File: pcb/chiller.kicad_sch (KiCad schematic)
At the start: 56 parts, among them J1 Temp sensor 1, J10 Current Sense, J11 Display, J12 Debug, J13 Conn_01x04, J14 Flow sensor, J15 Fan, J2 Temp sensor 2, J3 Ext, J4 Mains in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

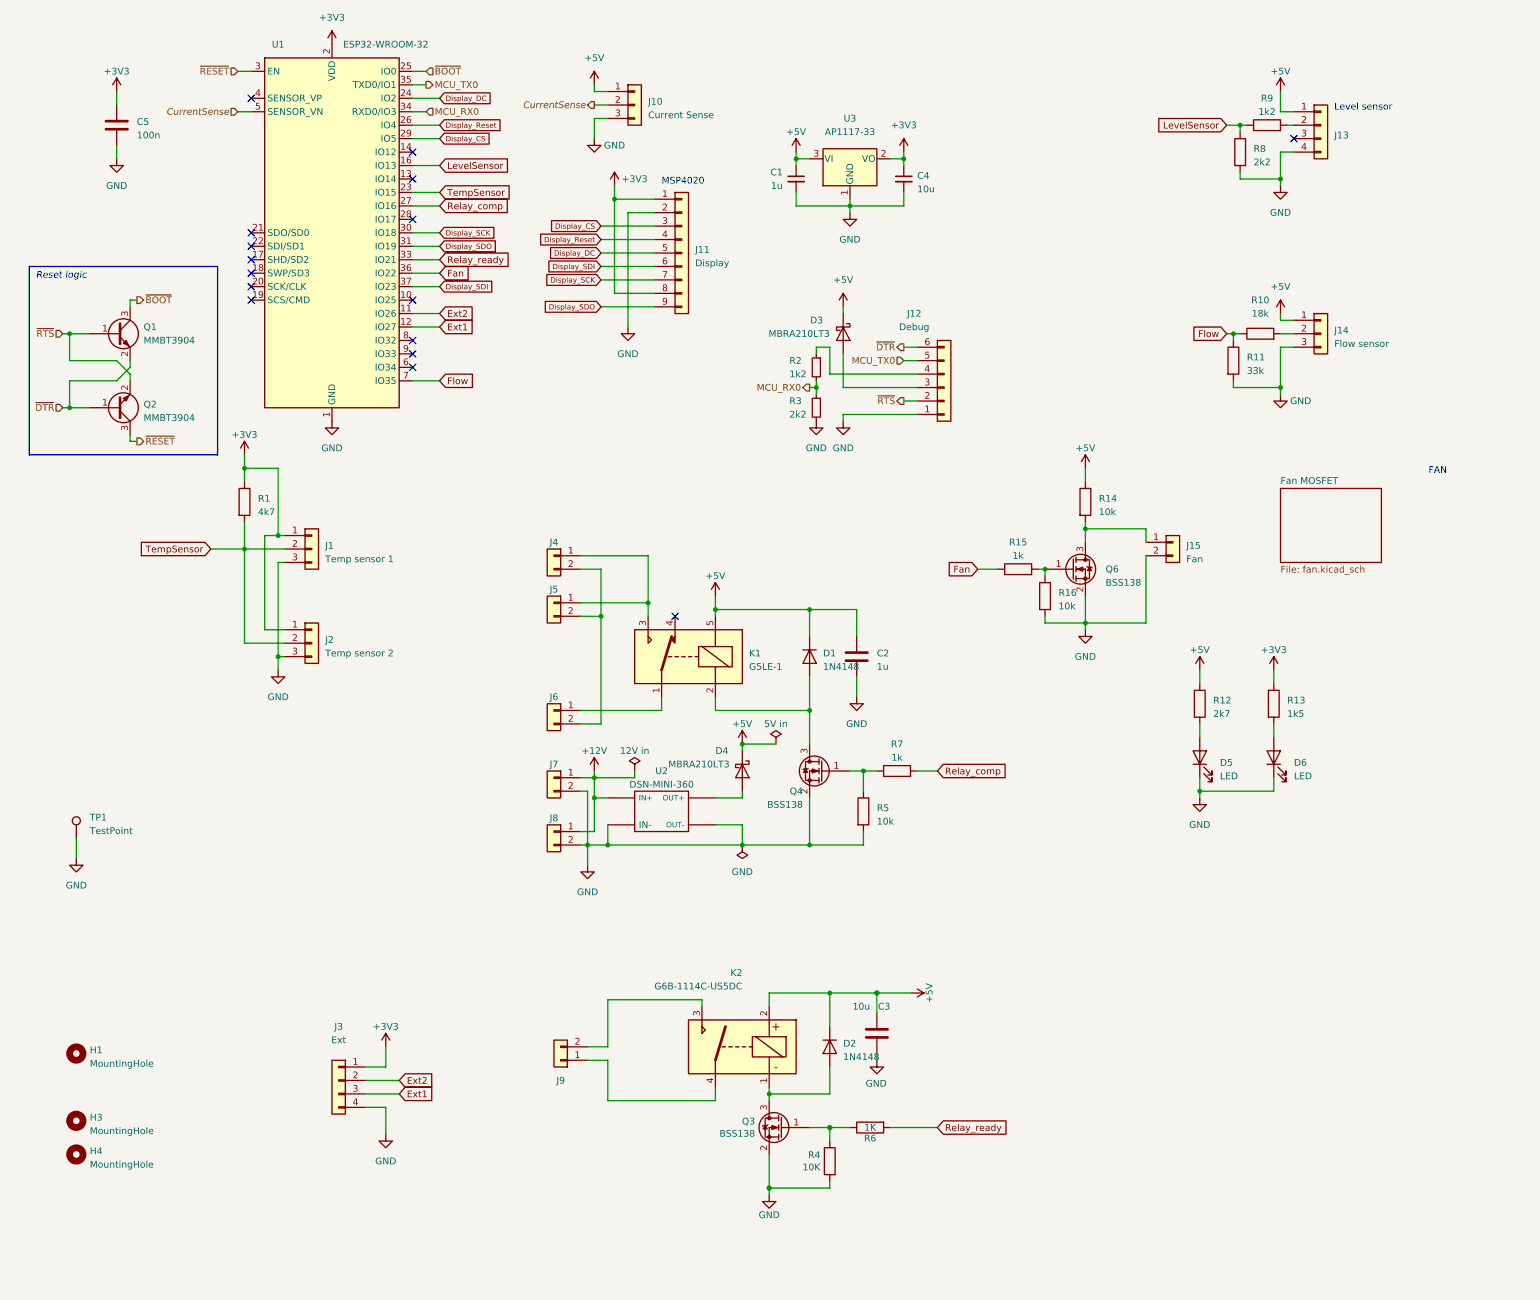
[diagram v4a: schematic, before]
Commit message: Add BOOT switch
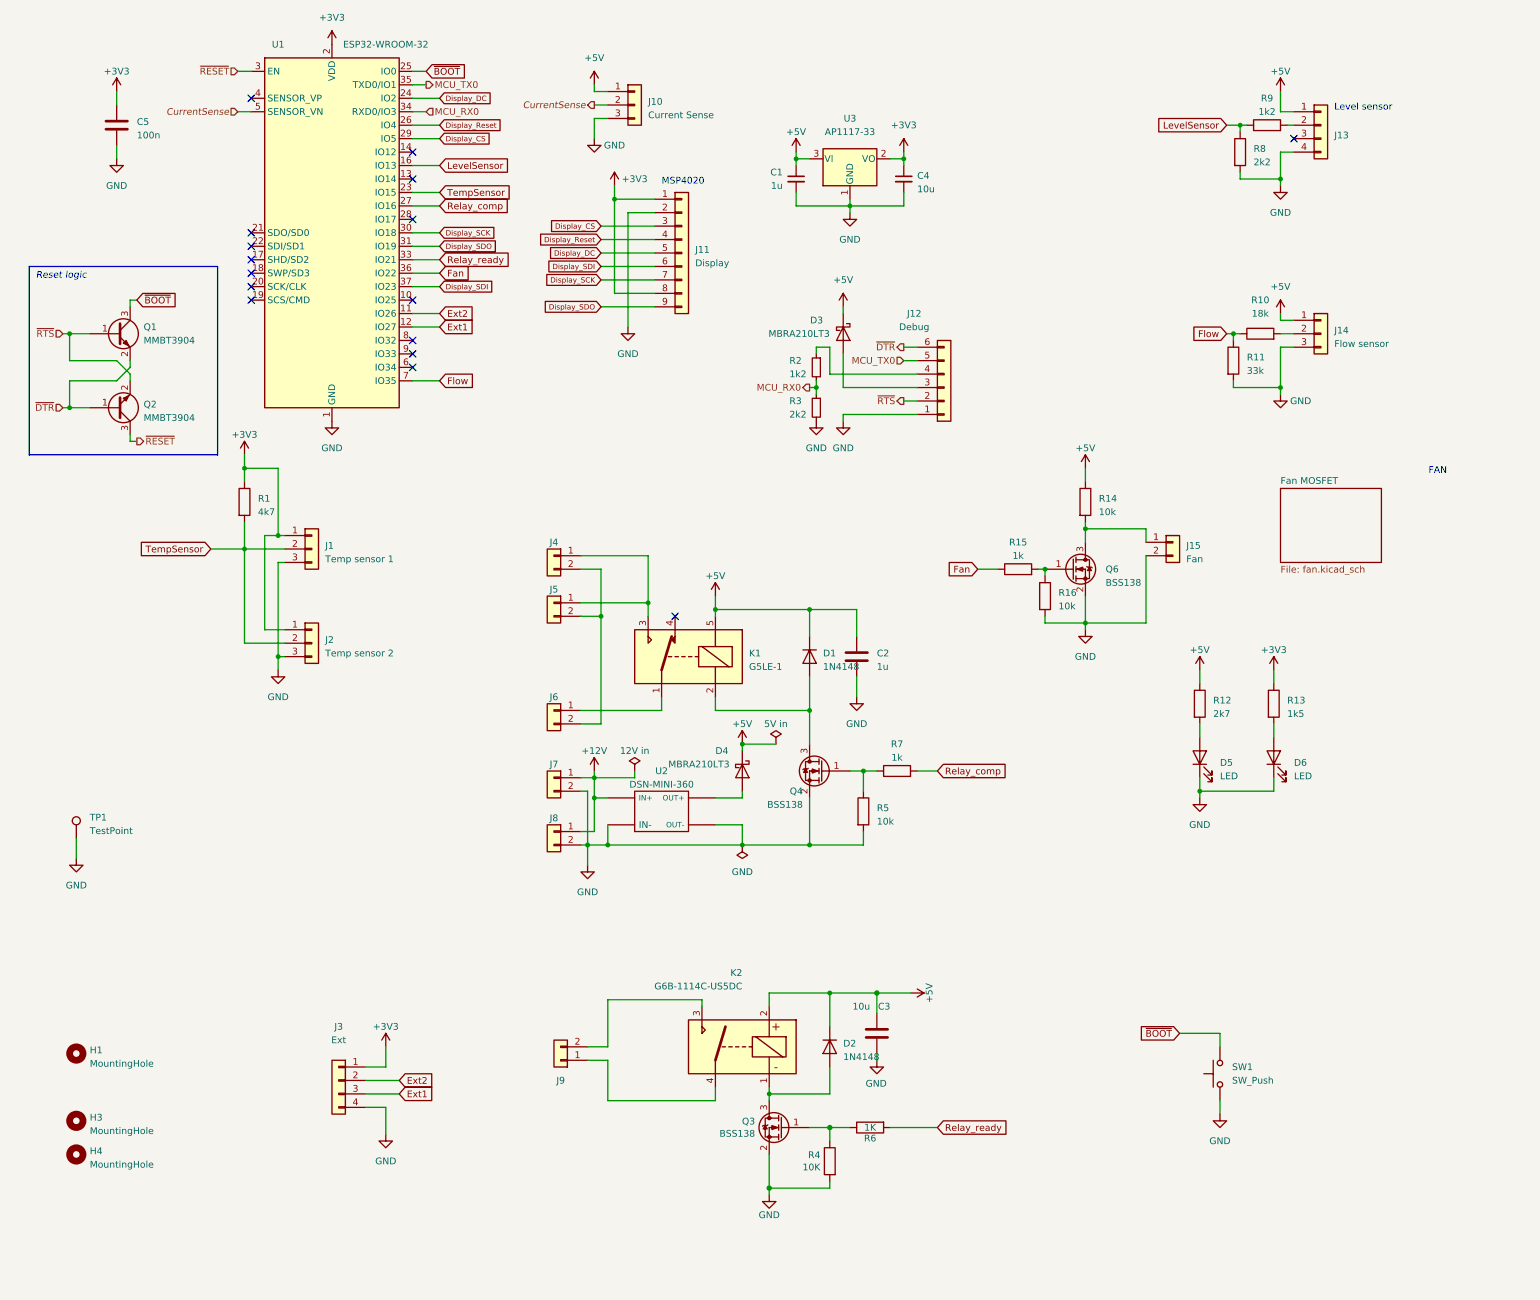
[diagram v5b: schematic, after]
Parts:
- added SW1: SW_Push, symbol Switch:SW_Push
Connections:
- net GND: now also SW1.1
- net ~{BOOT}: now also SW1.2
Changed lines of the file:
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@@
+    (stroke (width 0) (type default))
+  )
+  (wire (pts (xy 241.3 210.82) (xy 233.68 210.82))
     (stroke (width 0) (type default))
   )
@@
     (stroke (width 0) (type default))
   )
+  (wire (pts (xy 241.3 213.36) (xy 241.3 210.82))
+    (stroke (width 0) (type default))
+  )
   (wire (pts (xy 35.56 72.39) (xy 36.83 72.39))
     (stroke (width 0) (type default))
@@
   (wire (pts (xy 187.96 228.6) (xy 179.07 228.6))
     (stroke (width 0) (type solid))
+  )
+  (wire (pts (xy 241.3 223.52) (xy 241.3 226.06))
+    (stroke (width 0) (type default))
   )
   (wire (pts (xy 252.73 88.9) (xy 252.73 90.17))
@@
  (at 280.67 105.41 0)
     (effects (font (size 1.27 1.27)) (justify left bottom))
+  )
+  (global_label "~{BOOT}" (shape input) (at 36.83 72.39 0) (fields_autoplaced)
+    (effects (font (size 1.27 1.27)) (justify left))
+    (property "Intersheetrefs" "${INTERSHEET_REFS}" (at 44.7138 72.39 0)
+      (effects (font (size 1.27 1.27)) (justify left) hide)
+    )
   )
   (global_label "Relay_comp" (shape input) (at 93.98 54.61 0) (fields_autoplaced)
@@
     )
   )
+  (global_label "~{BOOT}" (shape input) (at 91.44 29.21 0) (fields_autoplaced)
+    (effects (font (size 1.27 1.27)) (justify left))
+    (property "Intersheetrefs" "${INTERSHEET_REFS}" (at 99.3238 29.21 0)
+      (effects (font (size 1.27 1.27)) (justify left) hide)
+    )
+  )
   (global_label "Display_Reset" (shape input) (at 93.98 39.37 0) (fields_autoplaced)
     (effects (font (size 1 1)) (justify left))
@@
     )
   )
+  (global_label "~{BOOT}" (shape input) (at 233.68 210.82 180) (fields_autoplaced)
+    (effects (font (size 1.27 1.27)) (justify right))
+    (property "Intersheetrefs" "${INTERSHEET_REFS}" (at 225.7962 210.82 0)
+      (effects (font (size 1.27 1.27)) (justify right) hide)
+    )
+  )
   (global_label "Display_DC" (shape input) (at 124.46 63.5 180) (fields_autoplaced)
     (effects (font (size 1 1)) (justify right))
@@
     (effects (font (size 1.27 1.27)) (justify right))
   )
-  (hierarchical_label "~{BOOT}" (shape output) (at 36.83 72.39 0) (fields_autoplaced)
-    (effects (font (size 1.27 1.27)) (justify left))
-  )
   (hierarchical_label "MCU_RX0" (shape output) (at 163.83 88.9 180) (fields_autoplaced)
     (effects (font (size 1.27 1.27)) (justify right))
@@
   (hierarchical_label "~{RTS}" (shape output) (at 181.61 91.44 180) (fields_autoplaced)
     (effects (font (size 1.27 1.27)) (justify right))
-  )
-  (hierarchical_label "~{BOOT}" (shape input) (at 91.44 29.21 0) (fields_autoplaced)
-    (effects (font (size 1.27 1.27)) (justify left))
   )
   (hierarchical_label "~{RTS}" (shape input) (at 22.86 78.74 180) (fields_autoplaced)
@@
     )
   )
+  (symbol (lib_id "Switch:SW_Push") (at 241.3 218.44 90) (unit 1)
+    (exclude_from_sim no) (in_bom yes) (on_board yes) (dnp no) (fields_autoplaced)
+    (property "Reference" "SW1" (at 243.586 217.1699 90)
+      (effects (font (size 1.27 1.27)) (justify right))
+    )
+    (property "Value" "SW_Push" (at 243.586 219.7099 90)
+      (effects (font (size 1.27 1.27)) (justify right))
+    )
+    (property "Footprint" "" (at 236.22 218.44 0)
+      (effects (font (size 1.27 1.27)) hide)
+    )
+    (property "Datasheet" "~" (at 236.22 218.44 0)
+      (effects (font (size 1.27 1.27)) hide)
+    )
+    (property "Description" "Push button switch, generic, two pins" (at 241.3 218.44 0)
+      (effects (font (size 1.27 1.27)) hide)
+    )
+    (pin "1")
+    (pin "2")
+    (instances
+      (project "chiller"
+        (path "/212a0d71-cc7b-49f8-b4ca-a935e5355dca"
+          (reference "SW1") (unit 1)
+        )
+      )
+    )
+  )
   (symbol (lib_id "Device:R_Small") (at 165.1 85.09 0) (mirror y) (unit 1)
     (exclude_from_sim no) (in_bom yes) (on_board yes) (dnp no)
@@
       (effects (font (size 1.27 1.27)) hide)
     )
-    (property "Description" "" (at 135.89 168.91 0)
+    (property "Description" "Linear Regulator +5V" (at 135.89 168.91 0)
       (effects (font (size 1.27 1.27)) hide)
     )
@@
         )
       )
+    )
+  )
+  (symbol (lib_id "power:GND") (at 241.3 226.06 0) (unit 1)
+    (exclude_from_sim no) (in_bom yes) (on_board yes) (dnp no) (fields_autoplaced)
+    (property "Reference" "#PWR035" (at 241.3 232.41 0)
+      (effects (font (size 1.27 1.27)) hide)
+    )
+    (property "Value" "GND" (at 241.3 231.14 0)
+      (effects (font (size 1.27 1.27)))
+    )
+    (property "Footprint" "" (at 241.3 226.06 0)
+      (effects (font (size 1.27 1.27)) hide)
+    )
+    (property "Datasheet" "" (at 241.3 226.06 0)
+      (effects (font (size 1.27 1.27)) hide)
+    )
+    (property "Description" "Power flag, ground" (at 241.3 226.06 0)
+      (effects (font (size 1.27 1.27)) hide)
+    )
+    (pin "1")
+    (instances
+      (project "chiller"
+        (path "/212a0d71-cc7b-49f8-b4ca-a935e5355dca"
+          (reference "#PWR035") (unit 1)
+        )
+      )

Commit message: Add addon board.
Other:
- removed sheet Fan MOSFET
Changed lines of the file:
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@@
-    )
-  )
-  (sheet (at 252.73 107.95) (size 19.05 13.97) (fields_autoplaced)
-    (stroke (width 0.1524) (type solid))
-    (fill (color 0 0 0 0.0000))
-    (property "Sheetname" "Fan MOSFET" (at 252.73 107.2384 0)
-      (effects (font (size 1.27 1.27)) (justify left bottom))
-    )
-    (property "Sheetfile" "fan.kicad_sch" (at 252.73 122.5046 0)
-      (effects (font (size 1.27 1.27)) (justify left top))
-    )
-    (instances
-      (project "chiller"
-        (path "/212a0d71-cc7b-49f8-b4ca-a935e5355dca" (page "2"))
-      )
     )
   )

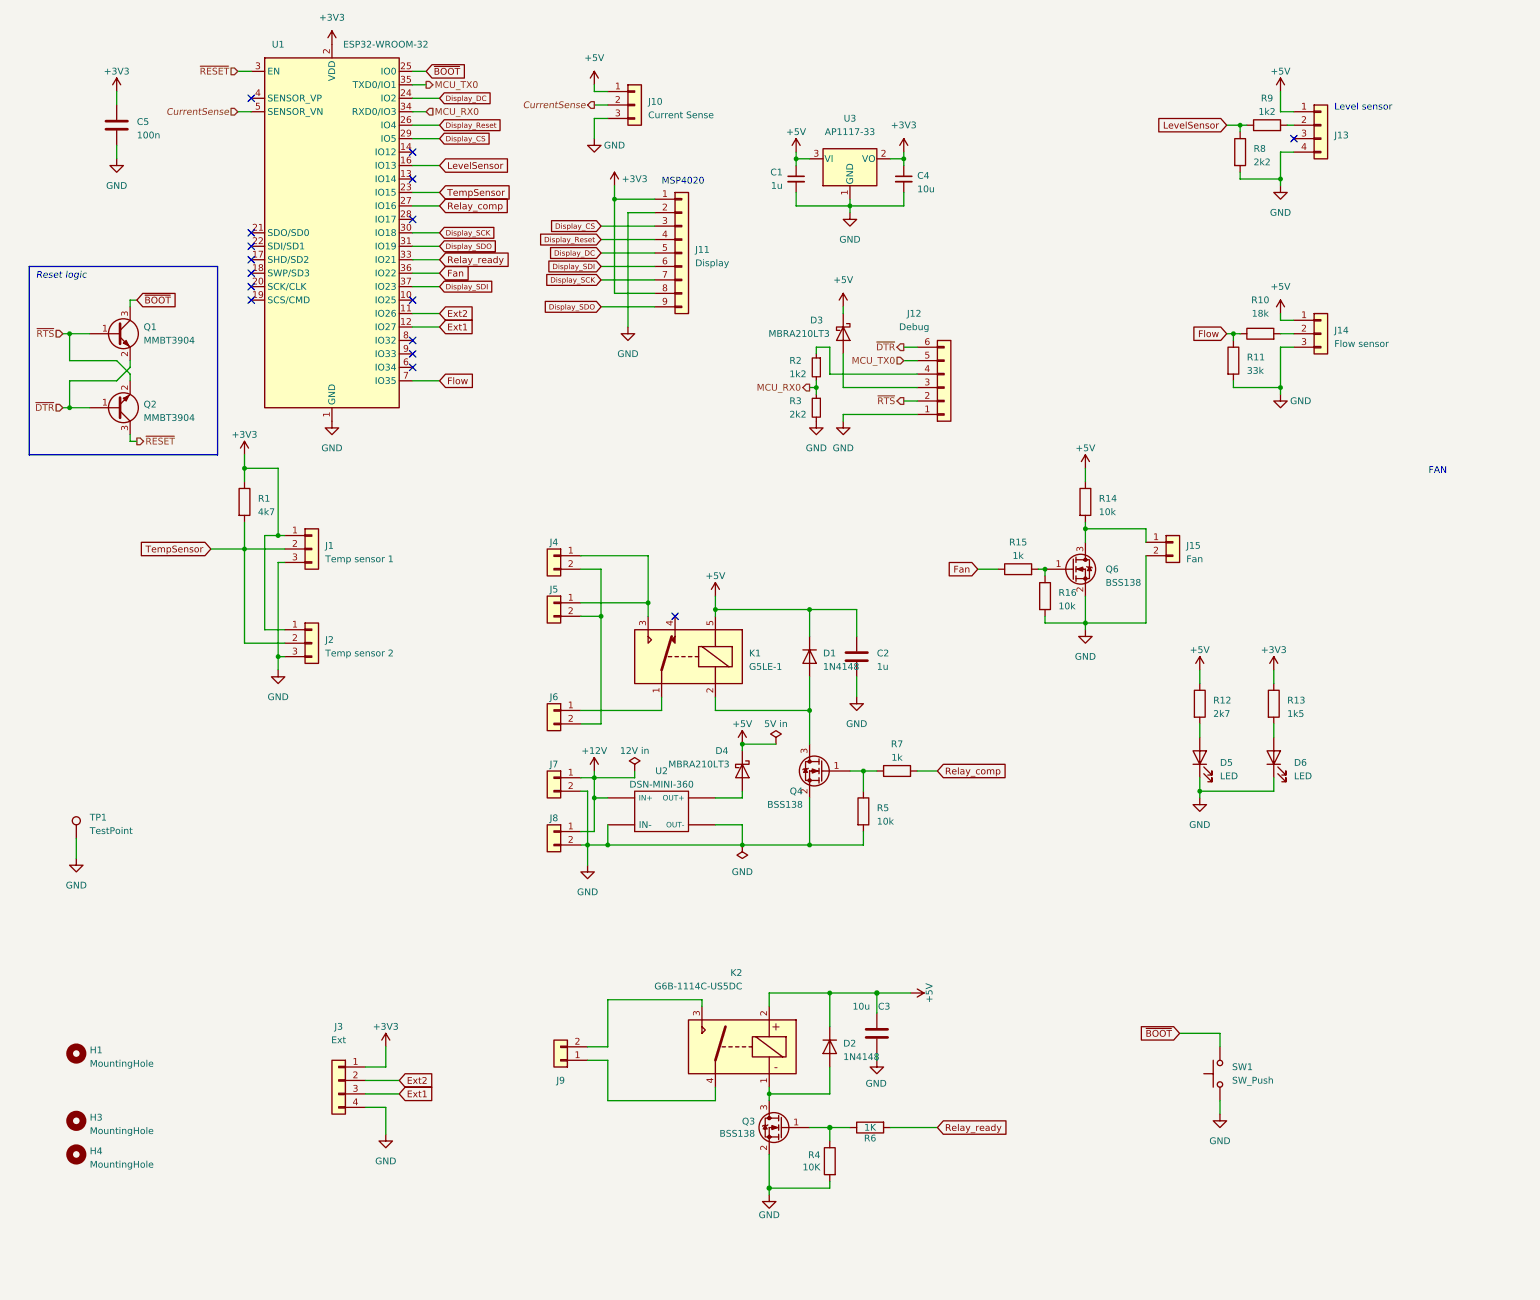
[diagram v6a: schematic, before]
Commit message: Move fan and buzzer MOSFETs onto main board.
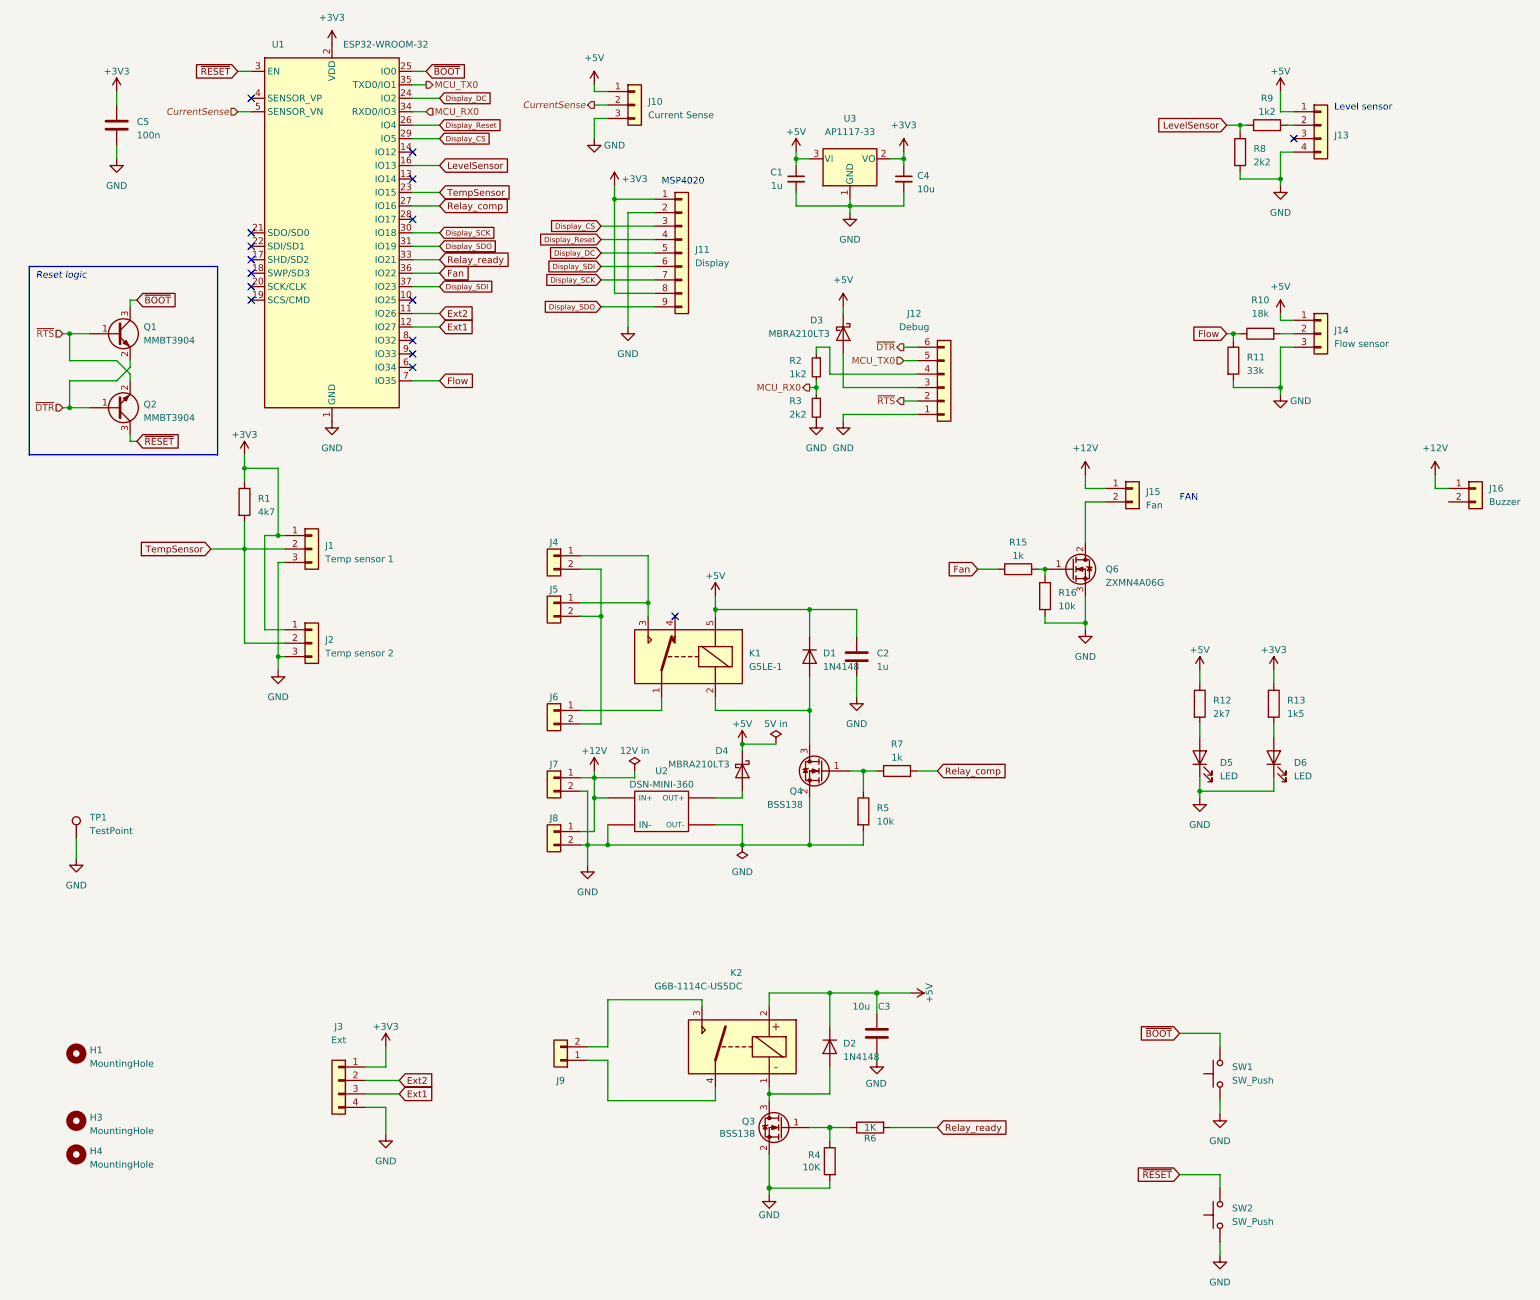
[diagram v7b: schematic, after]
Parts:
- removed R14: 10k, Resistor_SMD:R_0603_1608Metric, symbol Device:R
- added J16: Buzzer, symbol Connector_Generic:Conn_01x02
- added SW2: SW_Push, symbol Switch:SW_Push
- Q6: value BSS138 -> ZXMN4A06G; symbol Device:Q_NMOS_GSD -> Device:Q_NMOS_GDS
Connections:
- net +12V: now also J15.1 (Pin_1), J16.1 (Pin_1)
- net GND: now also Q6.3 (S), SW2.1; no longer J15.2 (Pin_2), Q6.2 (S)
- net ~{RESET}: now also SW2.2
- new net: J15.2 (Pin_2), Q6.2 (D)
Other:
- moved on the sheet: J15
